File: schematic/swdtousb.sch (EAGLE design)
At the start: 1 part

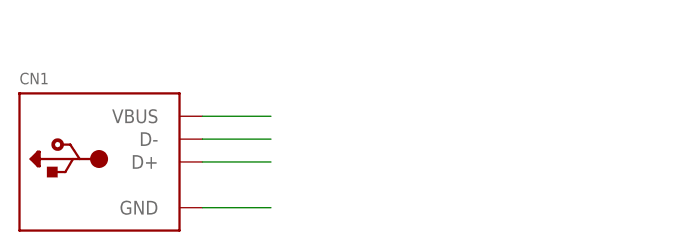
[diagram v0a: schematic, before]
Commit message: Finish design of swd->usb adapter
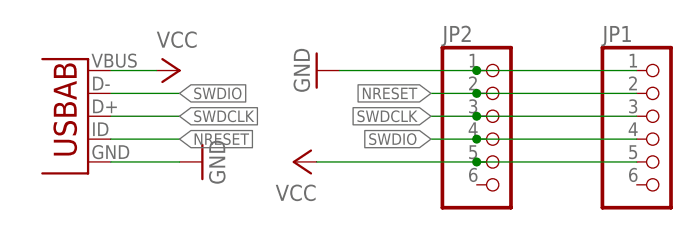
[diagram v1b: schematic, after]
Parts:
- removed CN1: (no value), microbuilder:USB_TYPEAPTHFML
- added JP1, JP2: (no value), adafruit:PINHD-1X6
- added U1: (no value), lightmeter:USB-AB
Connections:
- removed net N$1: CN1.VBUS
- removed net N$2: CN1.D-
- removed net N$3: CN1.D+
- removed net N$4: CN1.GND
- new net GND: JP1.1, JP2.1, U1.GND
- new net NRESET: JP1.2, JP2.2, U1.USBID
- new net SWDCLK: JP1.3, JP2.3, U1.D+
- new net SWDIO: JP1.4, JP2.4, U1.D-
- new net VCC: JP1.5, JP2.5, U1.VBUS
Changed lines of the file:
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@@
 <layer number="54" name="bGND_GNDA" color="1" fill="9" visible="yes" active="no"/>
 <layer number="56" name="wert" color="7" fill="1" visible="yes" active="no"/>
+<layer number="57" name="tCAD" color="7" fill="1" visible="no" active="no"/>
 <layer number="90" name="Modules" color="5" fill="1" visible="yes" active="yes"/>
 <layer number="91" name="Nets" color="2" fill="1" visible="yes" active="yes"/>
@@
 <layer number="97" name="Info" color="7" fill="1" visible="yes" active="yes"/>
 <layer number="98" name="Guide" color="6" fill="1" visible="yes" active="yes"/>
+<layer number="99" name="SpiceOrder" color="5" fill="1" visible="yes" active="yes"/>
 <layer number="100" name="Muster" color="7" fill="1" visible="yes" active="yes"/>
 <layer number="101" name="Patch_Top" color="12" fill="4" visible="yes" active="yes"/>
@@
 <layer number="111" name="MPL" color="7" fill="1" visible="yes" active="yes"/>
 <layer number="112" name="tSilk" color="7" fill="1" visible="yes" active="yes"/>
+<layer number="113" name="IDFDebug" color="4" fill="1" visible="yes" active="yes"/>
+<layer number="116" name="Patch_BOT" color="9" fill="4" visible="yes" active="yes"/>
 <layer number="121" name="sName" color="7" fill="1" visible="yes" active="yes"/>
 <layer number="122" name="_bPlace" color="7" fill="1" visible="yes" active="yes"/>
+<layer number="123" name="tTestmark" color="7" fill="1" visible="no" active="yes"/>
+<layer number="124" name="bTestmark" color="7" fill="1" visible="no" active="yes"/>
 <layer number="125" name="_tNames" color="7" fill="1" visible="yes" active="yes"/>
 <layer number="126" name="_bNames" color="7" fill="1" visible="yes" active="yes"/>
 <layer number="127" name="_tValues" color="7" fill="1" visible="yes" active="yes"/>
 <layer number="128" name="_bValues" color="7" fill="1" visible="yes" active="yes"/>
+<layer number="131" name="tAdjust" color="7" fill="1" visible="no" active="yes"/>
+<layer number="132" name="bAdjust" color="7" fill="1" visible="no" active="yes"/>
 <layer number="144" name="Drill_legend" color="7" fill="1" visible="yes" active="yes"/>
+<layer number="150" name="Notes" color="7" fill="1" visible="no" active="yes"/>
 <layer number="151" name="HeatSink" color="7" fill="1" visible="yes" active="yes"/>
 <layer number="152" name="_bDocu" color="7" fill="1" visible="yes" active="yes"/>
+<layer number="153" name="FabDoc1" color="6" fill="1" visible="no" active="no"/>
+<layer number="154" name="FabDoc2" color="2" fill="1" visible="no" active="no"/>
+<layer number="155" name="FabDoc3" color="7" fill="15" visible="no" active="no"/>
+<layer number="199" name="Contour" color="7" fill="1" visible="yes" active="yes"/>
 <layer number="200" name="200bmp" color="1" fill="10" visible="yes" active="yes"/>
 <layer number="201" name="201bmp" color="7" fill="1" visible="yes" active="yes"/>
@@
 <layer number="204" name="204bmp" color="7" fill="1" visible="yes" active="yes"/>
 <layer number="205" name="205bmp" color="7" fill="1" visible="yes" active="yes"/>
+<layer number="206" name="206bmp" color="7" fill="10" visible="yes" active="yes"/>
+<layer number="207" name="207bmp" color="8" fill="10" visible="yes" active="yes"/>
+<layer number="208" name="208bmp" color="9" fill="10" visible="yes" active="yes"/>
+<layer number="209" name="209bmp" color="7" fill="1" visible="no" active="yes"/>
+<layer number="210" name="210bmp" color="7" fill="1" visible="no" active="yes"/>
+<layer number="211" name="211bmp" color="7" fill="1" visible="yes" active="yes"/>
+<layer number="212" name="212bmp" color="7" fill="1" visible="yes" active="yes"/>
+<layer number="213" name="213bmp" color="7" fill="1" visible="yes" active="yes"/>
+<layer number="214" name="214bmp" color="7" fill="1" visible="yes" active="yes"/>
+<layer number="215" name="215bmp" color="7" fill="1" visible="yes" active="yes"/>
+<layer number="216" name="216bmp" color="7" fill="1" visible="yes" active="yes"/>
+<layer number="217" name="217bmp" color="18" fill="1" visible="no" active="no"/>
+<layer number="218" name="218bmp" color="19" fill="1" visible="no" active="no"/>
+<layer number="219" name="219bmp" color="20" fill="1" visible="no" active="no"/>
+<layer number="220" name="220bmp" color="21" fill="1" visible="no" active="no"/>
+<layer number="221" name="221bmp" color="22" fill="1" visible="no" active="no"/>
+<layer number="222" name="222bmp" color="23" fill="1" visible="no" active="no"/>
+<layer number="223" name="223bmp" color="24" fill="1" visible="no" active="no"/>
+<layer number="224" name="224bmp" color="25" fill="1" visible="no" active="no"/>
 <layer number="248" name="Housing" color="7" fill="1" visible="yes" active="yes"/>
 <layer number="249" name="Edge" color="7" fill="1" visible="yes" active="yes"/>
@@
 </classes>
 <parts>
-<part name="CN1" library="microbuilder" deviceset="USB_TYPEA" device="PTHFML"/>
+<part name="JP2" library="adafruit" deviceset="PINHD-1X6" device=""/>
+<part name="U1" library="lightmeter" deviceset="USB-AB" device=""/>
+<part name="GND2" library="supply1" deviceset="GND" device=""/>
+<part name="GND1" library="supply1" deviceset="GND" device=""/>
+<part name="P+1" library="supply1" deviceset="VCC" device=""/>
+<part name="JP1" library="adafruit" deviceset="PINHD-1X6" device=""/>
+<part name="P+2" library="supply1" deviceset="VCC" device=""/>
 </parts>
 <sheets>
@@
 </plain>
 <instances>
-<instance part="CN1" gate="G$1" x="55.88" y="58.42"/>
+<instance part="JP2" gate="A" x="99.06" y="60.96"/>
+<instance part="U1" gate="G$1" x="50.8" y="63.5" rot="R180"/>
+<instance part="GND2" gate="1" x="78.74" y="68.58" rot="R270"/>
+<instance part="GND1" gate="1" x="66.04" y="58.42" rot="R90"/>
+<instance part="P+1" gate="VCC" x="63.5" y="68.58" rot="R270"/>
+<instance part="JP1" gate="A" x="116.84" y="60.96"/>
+<instance part="P+2" gate="VCC" x="76.2" y="58.42" rot="R90"/>
 </instances>
 <busses>
 </busses>
 <nets>
-<net name="N$1" class="0">
+<net name="GND" class="0">
 <segment>
-<pinref part="CN1" gate="G$1" pin="VBUS"/>
-<wire x1="66.04" y1="63.5" x2="73.66" y2="63.5" width="0.1524" layer="91"/>
+<pinref part="JP2" gate="A" pin="1"/>
+<wire x1="96.52" y1="68.58" x2="81.28" y2="68.58" width="0.1524" layer="91"/>
+<pinref part="GND2" gate="1" pin="GND"/>
+<pinref part="JP1" gate="A" pin="1"/>
+<wire x1="96.52" y1="68.58" x2="114.3" y2="68.58" width="0.1524" layer="91"/>
+<junction x="96.52" y="68.58"/>
+</segment>
+<segment>
+<pinref part="U1" gate="G$1" pin="GND"/>
+<wire x1="55.88" y1="58.42" x2="63.5" y2="58.42" width="0.1524" layer="91"/>
+<pinref part="GND1" gate="1" pin="GND"/>
 </segment>
 </net>
-<net name="N$2" class="0">
+<net name="VCC" class="0">
 <segment>
-<pinref part="CN1" gate="G$1" pin="D-"/>
-<wire x1="66.04" y1="60.96" x2="73.66" y2="60.96" width="0.1524" layer="91"/>
+<pinref part="U1" gate="G$1" pin="VBUS"/>
+<wire x1="55.88" y1="68.58" x2="60.96" y2="68.58" width="0.1524" layer="91"/>
+<pinref part="P+1" gate="VCC" pin="VCC"/>
+</segment>
+<segment>
+<pinref part="JP2" gate="A" pin="5"/>
+<wire x1="96.52" y1="58.42" x2="78.74" y2="58.42" width="0.1524" layer="91"/>
+<pinref part="JP1" gate="A" pin="5"/>
+<wire x1="96.52" y1="58.42" x2="114.3" y2="58.42" width="0.1524" layer="91"/>
+<junction x="96.52" y="58.42"/>
+<pinref part="P+2" gate="VCC" pin="VCC"/>
 </segment>
 </net>
-<net name="N$3" class="0">
+<net name="SWDIO" class="0">
 <segment>
-<pinref part="CN1" gate="G$1" pin="D+"/>
-<wire x1="66.04" y1="58.42" x2="73.66" y2="58.42" width="0.1524" layer="91"/>
+<pinref part="U1" gate="G$1" pin="D-"/>
+<wire x1="55.88" y1="66.04" x2="63.5" y2="66.04" width="0.1524" layer="91"/>
+<label x="63.5" y="66.04" size="1.27" layer="95" xref="yes"/>
+</segment>
+<segment>
+<pinref part="JP2" gate="A" pin="4"/>
+<wire x1="96.52" y1="60.96" x2="91.44" y2="60.96" width="0.1524" layer="91"/>
+<label x="91.44" y="60.96" size="1.27" layer="95" rot="R180" xref="yes"/>
+<pinref part="JP1" gate="A" pin="4"/>
+<wire x1="96.52" y1="60.96" x2="114.3" y2="60.96" width="0.1524" layer="91"/>
+<junction x="96.52" y="60.96"/>
 </segment>
 </net>
-<net name="N$4" class="0">
+<net name="SWDCLK" class="0">
 <segment>
-<pinref part="CN1" gate="G$1" pin="GND"/>
-<wire x1="66.04" y1="53.34" x2="73.66" y2="53.34" width="0.1524" layer="91"/>
+<pinref part="U1" gate="G$1" pin="D+"/>
+<wire x1="55.88" y1="63.5" x2="63.5" y2="63.5" width="0.1524" layer="91"/>
+<label x="63.5" y="63.5" size="1.27" layer="95" xref="yes"/>
+</segment>
+<segment>
+<pinref part="JP2" gate="A" pin="3"/>
+<wire x1="96.52" y1="63.5" x2="91.44" y2="63.5" width="0.1524" layer="91"/>
+<label x="91.44" y="63.5" size="1.27" layer="95" rot="R180" xref="yes"/>
+<pinref part="JP1" gate="A" pin="3"/>
+<wire x1="96.52" y1="63.5" x2="114.3" y2="63.5" width="0.1524" layer="91"/>
+<junction x="96.52" y="63.5"/>
 </segment>
 </net>
+<net name="NRESET" class="0">
+<segment>
+<pinref part="U1" gate="G$1" pin="USBID"/>
+<wire x1="55.88" y1="60.96" x2="63.5" y2="60.96" width="0.1524" layer="91"/>
+<label x="63.5" y="60.96" size="1.27" layer="95" xref="yes"/>
+</segment>
+<segment>
+<pinref part="JP2" gate="A" pin="2"/>
+<pinref part="JP1" gate="A" pin="2"/>
+<wire x1="96.52" y1="66.04" x2="114.3" y2="66.04" width="0.1524" layer="91"/>
+<wire x1="96.52" y1="66.04" x2="91.44" y2="66.04" width="0.1524" layer="91"/>
+<junction x="96.52" y="66.04"/>
+<label x="91.44" y="66.04" size="1.27" layer="95" rot="R180" xref="yes"/>
+</segment>
+</net>
